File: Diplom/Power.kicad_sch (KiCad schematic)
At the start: 33 parts, among them Q1 SI2301, U4 SPV1040, U5 DW01A

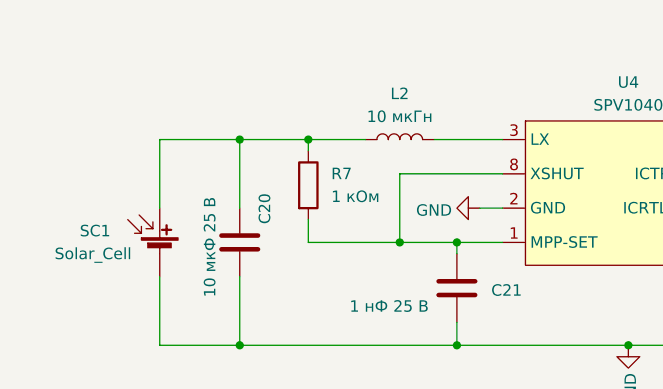
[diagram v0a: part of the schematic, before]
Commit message: version 2.0 fix buttons, roots, tighten dimension
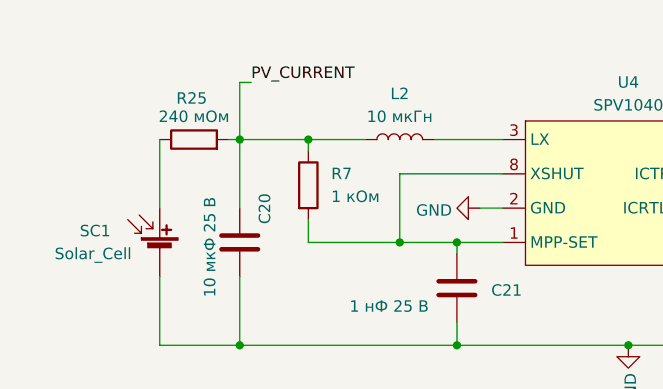
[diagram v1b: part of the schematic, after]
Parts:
- added R25: 240 мОм, Resistor_SMD:R_1206_3216Metric, symbol Device:R
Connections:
- net PV_CURRENT: now reaches C20.1, L2.1, R7.1
- net PV_CURRENT: now also R25.2; no longer SC1.1 (+)
- new net: R25.1, SC1.1 (+)
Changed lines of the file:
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@@
+	)
+	(junction
+		(at 118.11 88.9)
+		(diameter 0)
+		(color 0 0 0 0)
+	)
+	(junction
+		(at 138.43 54.61)
+		(diameter 0)
+		(color 0 0 0 0)
+	)
+	(junction
+		(at 124.46 101.6)
+		(diameter 0)
+		(color 0 0 0 0)
+	)
+	(junction
+		(at 66.04 43.18)
+		(diameter 0)
+		(color 0 0 0 0)
+	)
+	(junction
+		(at 41.91 54.61)
+		(diameter 0)
+		(color 0 0 0 0)
+	)
+	(junction
+		(at 161.29 110.49)
+		(diameter 0)
+		(color 0 0 0 0)
+	)
+	(junction
+		(at 43.18 80.01)
+		(diameter 0)
+		(color 0 0 0 0)
+	)
+	(junction
+		(at 172.72 87.63)
+		(diameter 0)
+		(color 0 0 0 0)
+	)
+	(junction
+		(at 31.75 88.9)
+		(diameter 0)
+		(color 0 0 0 0)
+	)
+	(junction
+		(at 49.53 31.75)
+		(diameter 0)
+		(color 0 0 0 0)
+	)
+	(junction
+		(at 66.04 54.61)
+		(diameter 0)
+		(color 0 0 0 0)
+	)
+	(junction
+		(at 179.07 87.63)
+		(diameter 0)
+		(color 0 0 0 0)
+	)
+	(junction
+		(at 31.75 80.01)
+		(diameter 0)
+		(color 0 0 0 0)
+	)
+	(junction
+		(at 59.69 43.18)
+		(diameter 0)
+		(color 0 0 0 0)
+	)
+	(junction
+		(at 172.72 78.74)
+		(diameter 0)
+		(color 0 0 0 0)
+	)
+	(junction
+		(at 138.43 43.18)
+		(diameter 0)
+		(color 0 0 0 0)
+	)
+	(junction
+		(at 138.43 31.75)
+		(diameter 0)
+		(color 0 0 0 0)
+	)
+	(junction
+		(at 100.33 54.61)
+		(diameter 0)
+		(color 0 0 0 0)
+	)
+	(junction
+		(at 146.05 31.75)
+		(diameter 0)
+		(color 0 0 0 0)
+	)
+	(junction
+		(at 111.76 31.75)
+		(diameter 0)
+		(color 0 0 0 0)
+	)
+	(junction
+		(at 165.1 95.25)
+		(diameter 0)
+		(color 0 0 0 0)
 	)
 	(junction
@@
 	)
 	(junction
-		(at 118.11 88.9)
-		(diameter 0)
-		(color 0 0 0 0)
-	)
-	(junction
-		(at 138.43 54.61)
-		(diameter 0)
-		(color 0 0 0 0)
-	)
-	(junction
-		(at 124.46 101.6)
-		(diameter 0)
-		(color 0 0 0 0)
-	)
-	(junction
-		(at 66.04 43.18)
-		(diameter 0)
-		(color 0 0 0 0)
-	)
-	(junction
-		(at 41.91 54.61)
-		(diameter 0)
-		(color 0 0 0 0)
-	)
-	(junction
-		(at 161.29 110.49)
-		(diameter 0)
-		(color 0 0 0 0)
-	)
-	(junction
-		(at 43.18 80.01)
-		(diameter 0)
-		(color 0 0 0 0)
-	)
-	(junction
-		(at 172.72 87.63)
-		(diameter 0)
-		(color 0 0 0 0)
-	)
-	(junction
-		(at 31.75 88.9)
-		(diameter 0)
-		(color 0 0 0 0)
-	)
-	(junction
-		(at 49.53 31.75)
-		(diameter 0)
-		(color 0 0 0 0)
-	)
-	(junction
-		(at 66.04 54.61)
-		(diameter 0)
-		(color 0 0 0 0)
-	)
-	(junction
-		(at 179.07 87.63)
-		(diameter 0)
-		(color 0 0 0 0)
-	)
-	(junction
-		(at 31.75 80.01)
-		(diameter 0)
-		(color 0 0 0 0)
-	)
-	(junction
-		(at 59.69 43.18)
-		(diameter 0)
-		(color 0 0 0 0)
-	)
-	(junction
-		(at 172.72 78.74)
-		(diameter 0)
-		(color 0 0 0 0)
-	)
-	(junction
-		(at 138.43 43.18)
-		(diameter 0)
-		(color 0 0 0 0)
-	)
-	(junction
-		(at 138.43 31.75)
-		(diameter 0)
-		(color 0 0 0 0)
-	)
-	(junction
-		(at 100.33 54.61)
-		(diameter 0)
-		(color 0 0 0 0)
-	)
-	(junction
-		(at 146.05 31.75)
-		(diameter 0)
-		(color 0 0 0 0)
-	)
-	(junction
-		(at 111.76 31.75)
-		(diameter 0)
-		(color 0 0 0 0)
-	)
-	(junction
-		(at 165.1 95.25)
-		(diameter 0)
-		(color 0 0 0 0)
-	)
-	(junction
 		(at 76.2 101.6)
 		(diameter 0)
@@
 	(wire
 		(pts
+			(xy 41.91 25.4) (xy 41.91 31.75)
+		)
+		(stroke
+			(width 0)
+			(type default)
+		)
+	)
+	(wire
+		(pts
 			(xy 55.88 31.75) (xy 49.53 31.75)
 		)
@@
 	(wire
 		(pts
+			(xy 40.64 31.75) (xy 41.91 31.75)
+		)
+		(stroke
+			(width 0)
+			(type default)
+		)
+	)
+	(wire
+		(pts
 			(xy 118.11 31.75) (xy 120.65 31.75)
 		)
@@
 	(wire
 		(pts
-			(xy 33.02 31.75) (xy 41.91 31.75)
-		)
-		(stroke
-			(width 0)
-			(type default)
-		)
-	)
-	(wire
-		(pts
 			(xy 158.75 106.68) (xy 161.29 106.68)
 		)
@@
 		(pts
 			(xy 31.75 88.9) (xy 43.18 88.9)
+		)
+		(stroke
+			(width 0)
+			(type default)
+		)
+	)
+	(wire
+		(pts
+			(xy 43.18 25.4) (xy 41.91 25.4)
 		)
 		(stroke
@@
 	(label "VBAT+"
 		(at 82.55 73.66 0)
+		(effects
+			(font
+				(size 1.27 1.27)
+			)
+			(justify left bottom)
+		)
+	)
+	(label "PV_CURRENT"
+		(at 43.18 25.4 0)
 		(effects
 			(font
@@
 					(unit 1)
 				)
+			)
+		)
+	)
+	(symbol
+		(lib_id "Device:R")
+		(at 36.83 31.75 90)
+		(unit 1)
+		(exclude_from_sim no)
+		(in_bom yes)
+		(on_board yes)
+		(dnp no)
+		(property "Reference" "R25"
+			(at 36.576 27.178 90)
+			(effects
+				(font
+					(size 1.27 1.27)
+				)
+			)
+		)
+		(property "Value" "240 мОм"
+			(at 36.83 29.21 90)
+			(effects
+				(font
+					(size 1.27 1.27)
+				)
+			)
+		)
+		(property "Footprint" "Resistor_SMD:R_1206_3216Metric"
+			(at 36.83 33.528 90)
+			(effects
+				(font
+					(size 1.27 1.27)
+				)
+				(hide yes)
+			)
+		)
+		(property "Datasheet" "~"
+			(at 36.83 31.75 0)
+			(effects
+				(font
+					(size 1.27 1.27)
+				)
+				(hide yes)
+			)
+		)
+		(property "Description" "Resistor"
+			(at 36.83 31.75 0)
+			(effects
+				(font
+					(size 1.27 1.27)
+				)
+				(hide yes)
+			)
+		)
+		(pin "1"
+		)
+		(pin "2"
+		)
+		(instances
+			(project "Diplom"
+				(path "/c3b9ff52-a8d6-450c-a11b-f6a6738b7917/8f44266c-164d-4080-a485-6c50fd5299b8"
+					(reference "R25")
+					(unit 1)
+				)

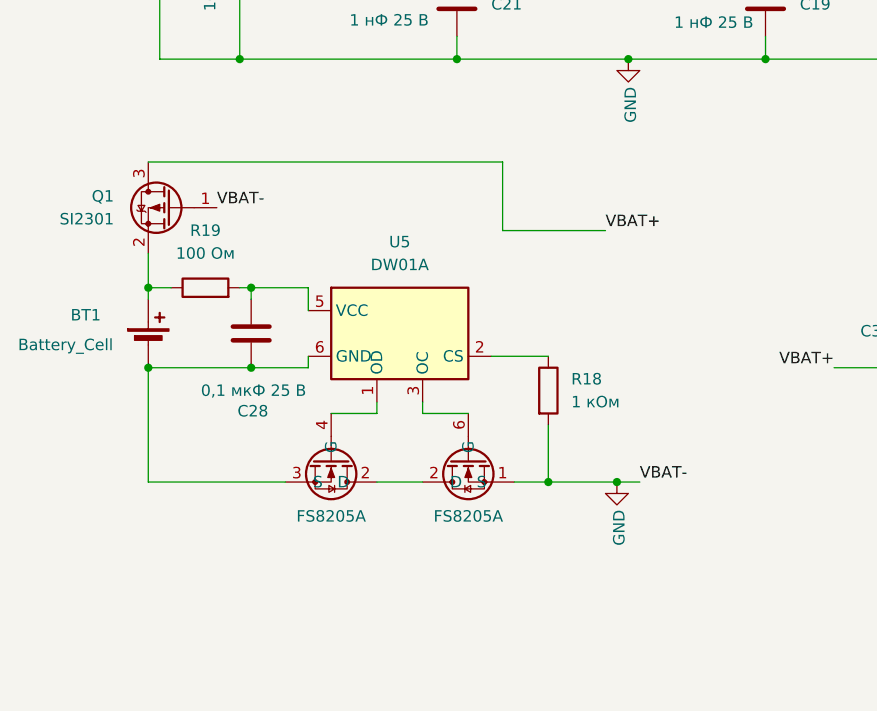
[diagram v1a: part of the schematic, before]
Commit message: Исправил место под кварц 25МГц, заменил батарею на пакет, перевернул лору. Сырая компоновка без разводки
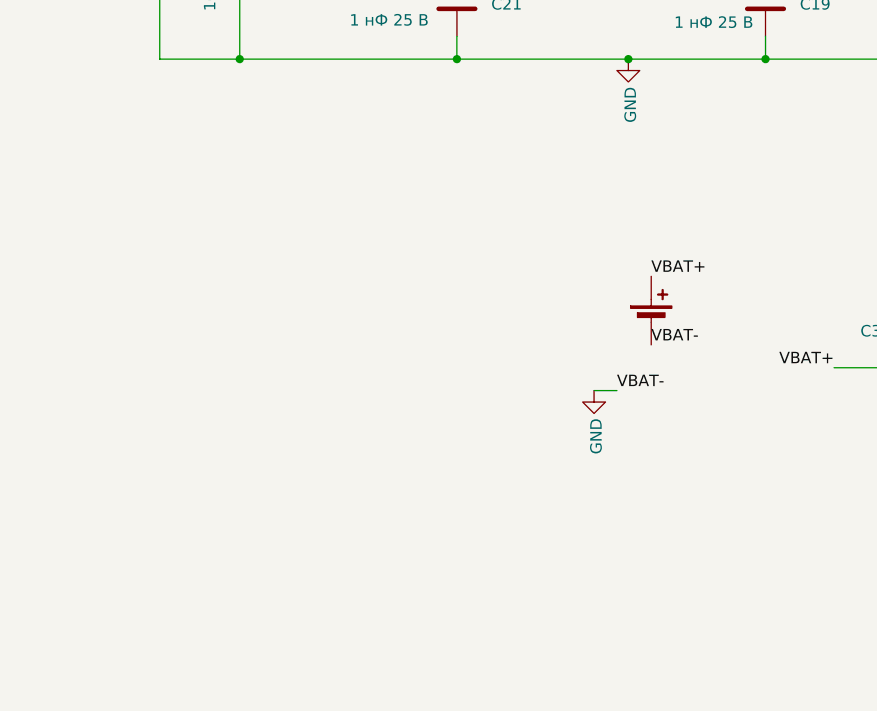
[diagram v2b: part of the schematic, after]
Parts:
- removed C28: 0,1 мкФ 25 В, Capacitor_SMD:C_0603_1608Metric_Pad1.08x0.95mm_HandSolder, symbol Device:C
- removed D4: FS8205A, Package_TO_SOT_SMD:SOT-23-6_Handsoldering, symbol Diplom:FS8205A
- removed Q1: SI2301, Package_TO_SOT_SMD:SOT-23, symbol Transistor_FET:BSS84
- removed R18: 1 кОм, Resistor_SMD:R_0603_1608Metric_Pad0.98x0.95mm_HandSolder, symbol Device:R
- removed R19: 100 Ом, Resistor_SMD:R_0603_1608Metric_Pad0.98x0.95mm_HandSolder, symbol Device:R
- removed U5: DW01A, Package_TO_SOT_SMD:SOT-23-6, symbol Battery_Management:DW01A
- BT1: footprint Battery:BatteryHolder_MPD_BH-18650-PC2 -> Connector_Wire:SolderWire-0.75sqmm_1x02_P4.8mm_D1.25mm_OD2.3mm
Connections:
- net GND: now also BT1.2 (-)
- net VBAT+: now also BT1.1 (+)
